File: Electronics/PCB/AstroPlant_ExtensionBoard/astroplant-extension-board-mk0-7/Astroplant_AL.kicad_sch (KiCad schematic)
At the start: 25 parts, among them J1 JST_XH_Relays, J10 JST_XH_UART, J11 JST_HX_2, J2 2x40 2.5mm Header, J3 JST-XH_3, J4 JST-XH_3, J5 JST_HX_2, J7 JST-XH_3, J8 JST_HX_2, J9 JST-XH_3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

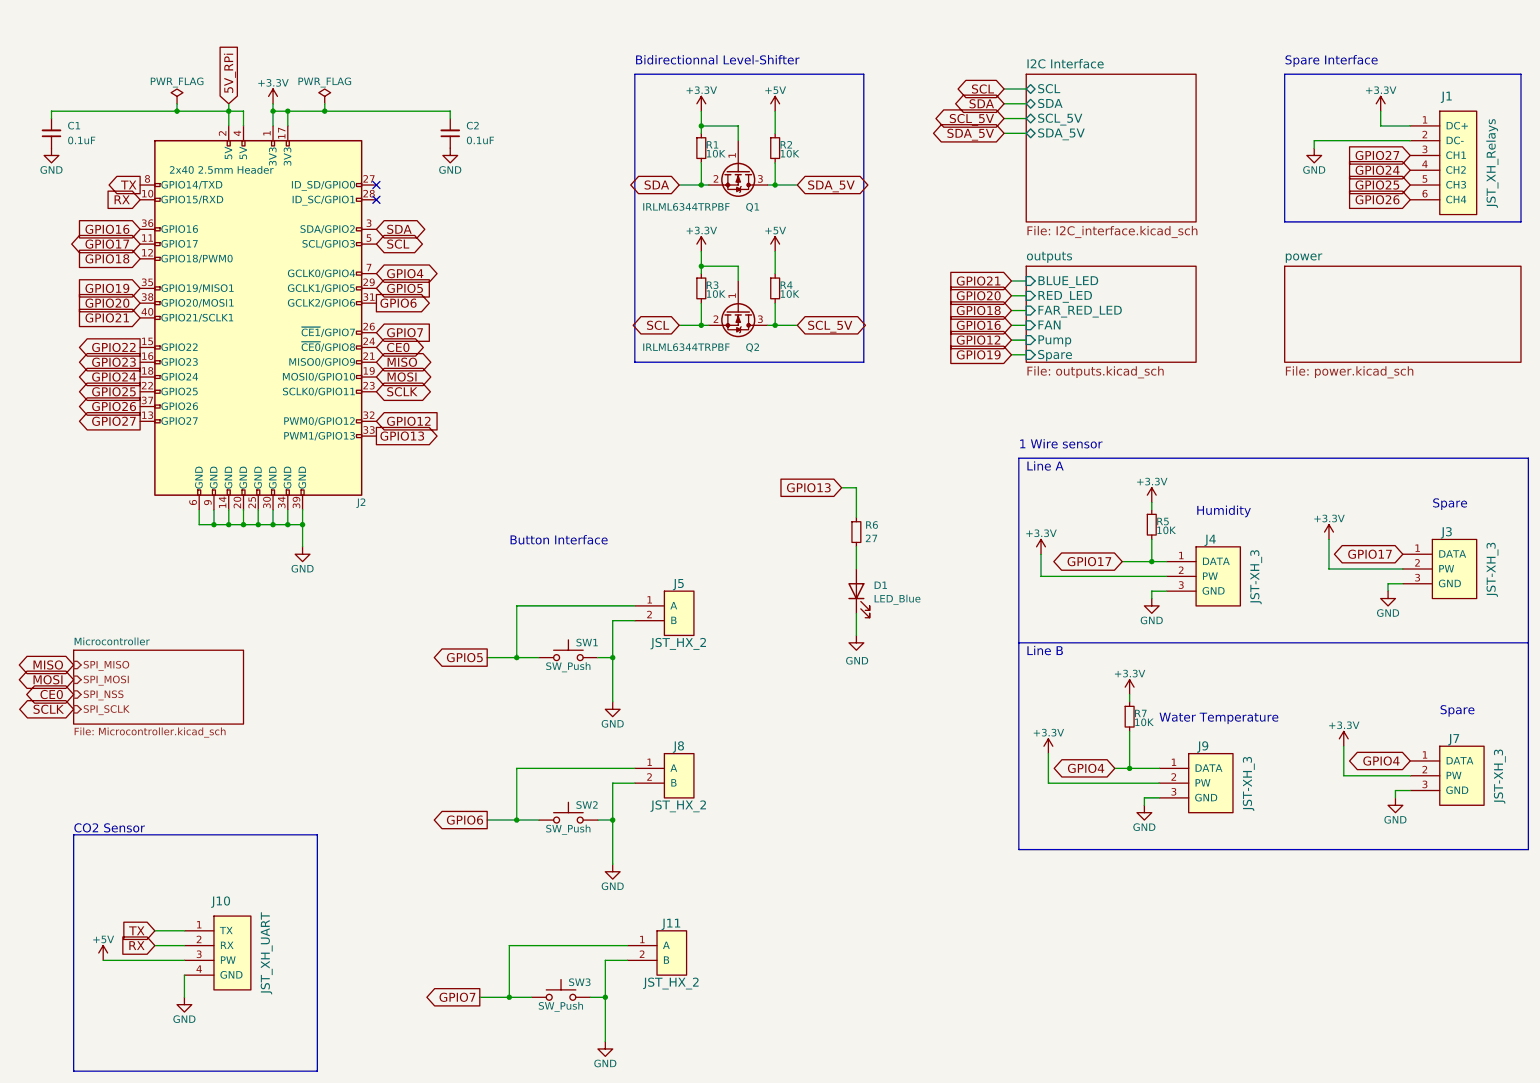
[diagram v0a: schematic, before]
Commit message: Update schematic and change library path
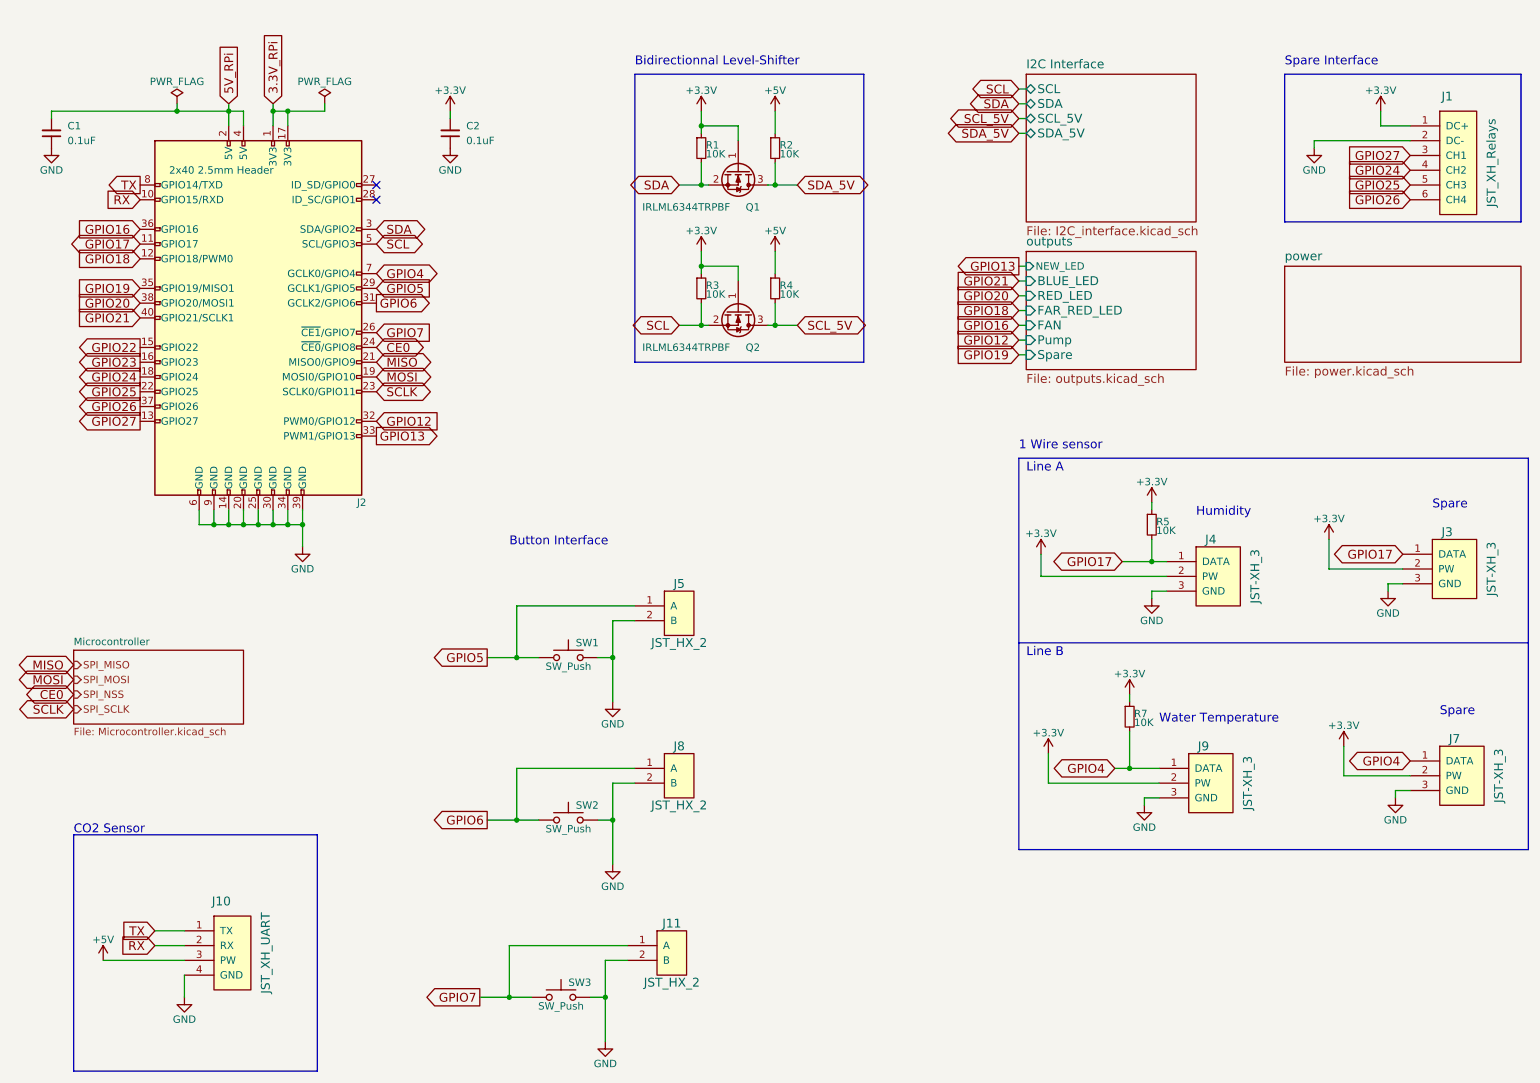
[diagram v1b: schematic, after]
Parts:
- removed D1: LED_Blue, LED_SMD:LED_0603_1608Metric, symbol Device:LED
- removed R6: 27, Resistor_SMD:R_0603_1608Metric, symbol Device:R_Small
- J1: footprint Connector_JST:JST_XH_B06B-XH-A_1x06_P2.50mm_Vertical -> SamacSys_Parts:SHDR6W64P0X250_1X6_1740X575X700P
- J10: footprint Connector_JST:JST_XH_B04B-XH-A_1x04_P2.50mm_Vertical -> SamacSys_Parts:B4BXHALFSN
- J11, J5, J8: footprint Connector_JST:JST_XH_B02B-XH-A_1x02_P2.50mm_Vertical -> SamacSys_Parts:SHDR2W64P0X250_1X2_740X575X700P
- J2: footprint footprints:Pin_Header_Straight_2x20_Pitch2.54mm -> SamacSys_Parts:HDRV40W64P254X254_2X20_5080X508X869P
- J3, J4, J7, J9: footprint Connector_JST:JST_XH_B03B-XH-A_1x03_P2.50mm_Vertical -> SamacSys_Parts:B3BXHALFSN
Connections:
- net +3V3: no longer J2.1 (3V3), J2.17 (3V3)
- new net 3.3V_RPi: J2.1 (3V3), J2.17 (3V3)
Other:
- sheet outputs ports: added NEW_LED; removed none

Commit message: Place components on PCB
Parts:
- removed C1, C2: 0.1uF, Capacitor_SMD:C_0805_2012Metric, symbol Device:C_Small
- removed R1, R2, R3, R4, R5, R7: 10K, Resistor_SMD:R_0805_2012Metric, symbol Device:R_Small
- added C9 (x2): 100nF, Capacitor_SMD:C_0603_1608Metric, symbol Device:C_Small
- added R24 (x6): 10k, Resistor_SMD:R_0603_1608Metric, symbol Device:R_Small
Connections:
- net +3V3: now also C9.1, R24.2, R24.2, R24.2, R24.2
- net +5V: now also R24.2, R24.2
- net 5V_RPi: now also C9.1
- net GND: now also C9.2, C9.2
- net GPIO17: now also R24.1
- net GPIO4: now also R24.1
- net SCL: now also R24.1
- net SCL_5V: now also R24.1
- net SDA: now also R24.1
- net SDA_5V: now also R24.1

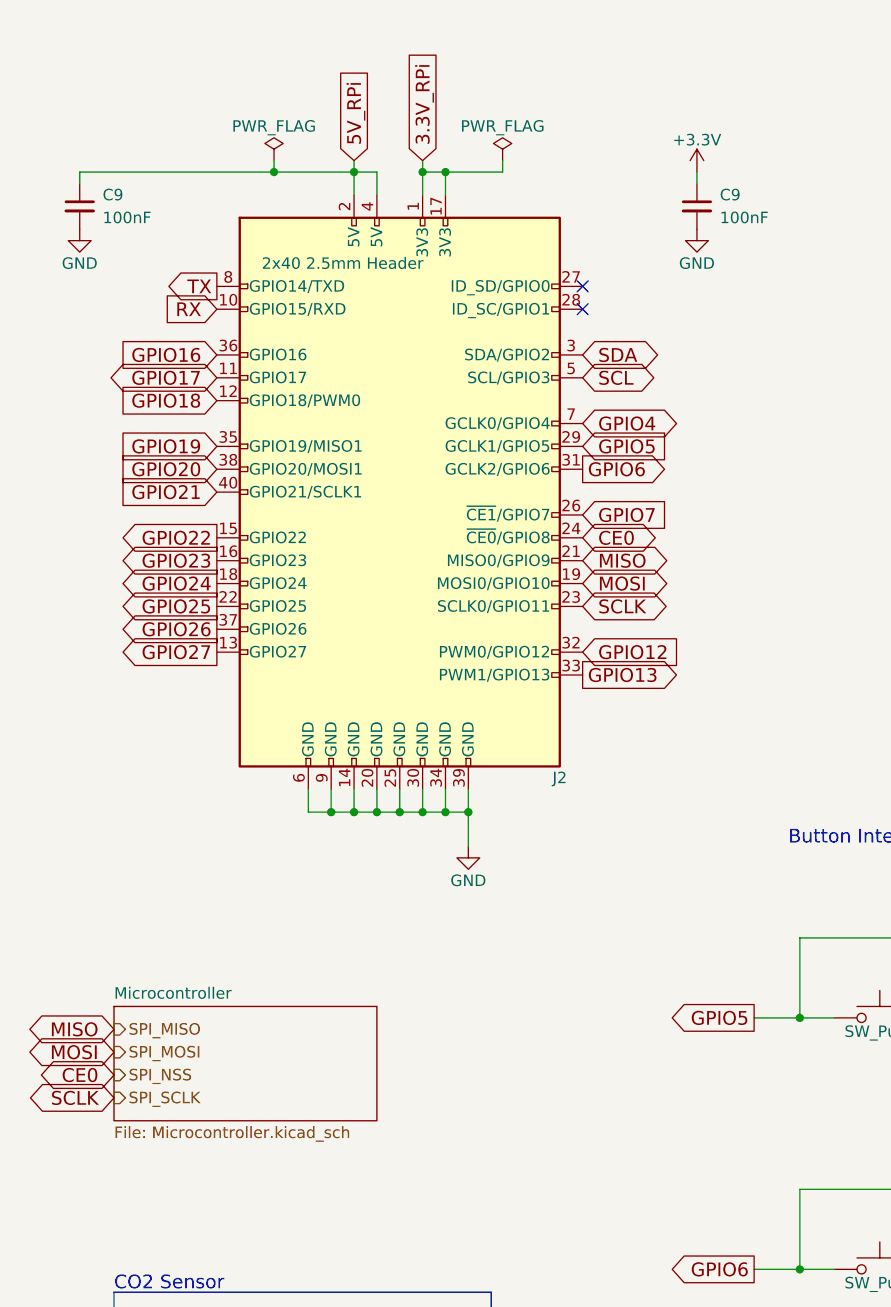
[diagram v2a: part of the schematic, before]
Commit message: Add route to PCB
Not the final version of the PCB, missing components for the antenna and also non-component things like the astroplant logo, the version and placement of the component designators.
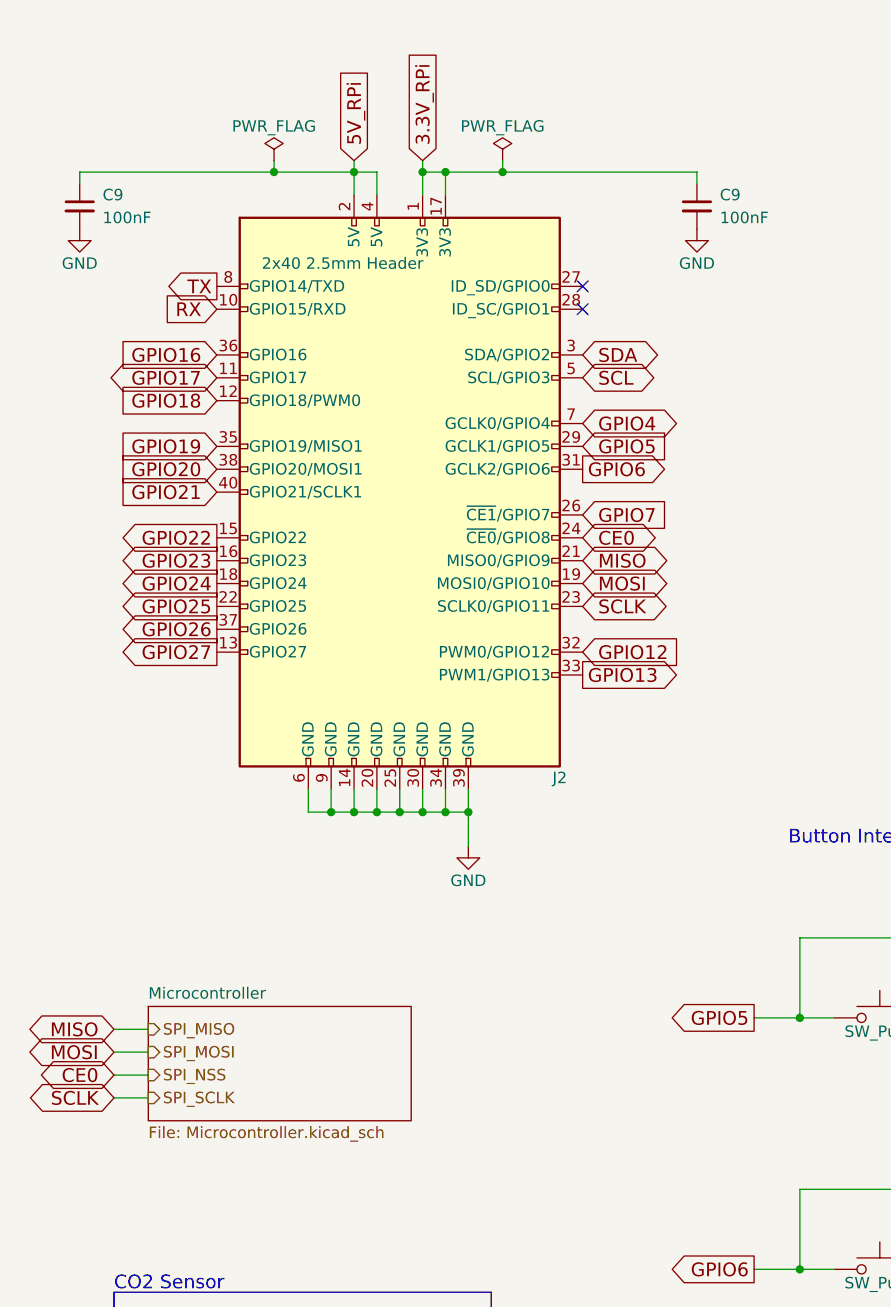
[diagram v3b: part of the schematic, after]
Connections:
- net +3V3: no longer C9.1
- net 3.3V_RPi: now also C9.1
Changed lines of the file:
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@@
   (junction (at 116.84 123.19) (diameter 0) (color 0 0 0 0)
+  )
+  (junction (at 67.31 29.21) (diameter 0) (color 0 0 0 0)
   )
   (junction (at 132.08 55.88) (diameter 0) (color 0 0 0 0)
@@
     (stroke (width 0) (type default))
   )
+  (wire (pts (xy 27.94 129.54) (xy 24.13 129.54))
+    (stroke (width 0) (type default))
+  )
   (wire (pts (xy 63.5 97.79) (xy 63.5 100.33))
     (stroke (width 0) (type default))
@@
     (stroke (width 0) (type default))
   )
+  (wire (pts (xy 27.94 124.46) (xy 24.13 124.46))
+    (stroke (width 0) (type default))
+  )
   (wire (pts (xy 132.08 62.23) (xy 132.08 66.04))
     (stroke (width 0) (type default))
   )
+  (wire (pts (xy 27.94 132.08) (xy 24.13 132.08))
+    (stroke (width 0) (type default))
+  )
   (wire (pts (xy 60.96 29.21) (xy 67.31 29.21))
     (stroke (width 0) (type default))
@@
     (stroke (width 0) (type default))
   )
+  (wire (pts (xy 27.94 127) (xy 24.13 127))
+    (stroke (width 0) (type default))
+  )
   (wire (pts (xy 50.8 100.33) (xy 50.8 97.79))
     (stroke (width 0) (type default))
@@
     (stroke (width 0) (type default))
   )
-  (wire (pts (xy 88.9 29.21) (xy 88.9 30.48))
-    (stroke (width 0) (type default))
-  )
   (wire (pts (xy 60.96 100.33) (xy 60.96 97.79))
     (stroke (width 0) (type default))
@@
     (stroke (width 0) (type default))
   )
+  (wire (pts (xy 88.9 30.48) (xy 88.9 29.21))
+    (stroke (width 0) (type default))
+  )
   (wire (pts (xy 114.3 151.13) (xy 116.84 151.13))
     (stroke (width 0) (type default))
@@
   )
   (polyline (pts (xy 186.69 88.9) (xy 186.69 156.21))
+    (stroke (width 0) (type default))
+  )
+  (wire (pts (xy 88.9 29.21) (xy 67.31 29.21))
     (stroke (width 0) (type default))
   )
@@
     )
   )
-  (hierarchical_label "SPI_MISO" (shape output) (at 24.13 124.46 0) (fields_autoplaced)
+  (hierarchical_label "SPI_MISO" (shape output) (at 27.94 124.46 0) (fields_autoplaced)
     (effects (font (size 1.27 1.27)) (justify left))
   )
-  (hierarchical_label "SPI_SCLK" (shape output) (at 24.13 132.08 0) (fields_autoplaced)
+  (hierarchical_label "SPI_SCLK" (shape output) (at 27.94 132.08 0) (fields_autoplaced)
     (effects (font (size 1.27 1.27)) (justify left))
   )
-  (hierarchical_label "SPI_NSS" (shape output) (at 24.13 129.54 0) (fields_autoplaced)
+  (hierarchical_label "SPI_NSS" (shape output) (at 27.94 129.54 0) (fields_autoplaced)
     (effects (font (size 1.27 1.27)) (justify left))
   )
-  (hierarchical_label "SPI_MOSI" (shape output) (at 24.13 127 0) (fields_autoplaced)
+  (hierarchical_label "SPI_MOSI" (shape output) (at 27.94 127 0) (fields_autoplaced)
     (effects (font (size 1.27 1.27)) (justify left))
   )
@@
     )
   )
-  (symbol (lib_id "Astroplant_VFR-rescue:+3.3V-power") (at 88.9 29.21 0) (unit 1)
-    (in_bom yes) (on_board yes) (dnp no)
-    (property "Reference" "#PWR0116" (at 88.9 33.02 0)
-      (effects (font (size 1.27 1.27)) hide)
-    )
-    (property "Value" "+3.3V" (at 88.9 25.654 0)
-      (effects (font (size 1.27 1.27)))
-    )
-    (property "Footprint" "" (at 88.9 29.21 0)
-      (effects (font (size 1.27 1.27)) hide)
-    )
-    (property "Datasheet" "" (at 88.9 29.21 0)
-      (effects (font (size 1.27 1.27)) hide)
-    )
-    (pin "1")
-    (instances
-      (project "Astroplant_VFR"
-        (path "/4e818498-015c-45b7-982b-80c19490efdc"
-          (reference "#PWR0116") (unit 1)
-        )
-      )
-      (project "Astroplant_AL"
-        (path "/51acab52-3cd6-4bba-9dee-c12efd332038"
-          (reference "#PWR014") (unit 1)
-        )
-        (path "/51acab52-3cd6-4bba-9dee-c12efd332038/5f0c961f-7fa6-4a15-8a74-755a432cc19e"
-          (reference "#PWR06") (unit 1)
-        )
-        (path "/51acab52-3cd6-4bba-9dee-c12efd332038/00000000-0000-0000-0000-00005a8053d4"
-          (reference "#PWR011") (unit 1)
-        )
-      )
-    )
-  )
   (symbol (lib_id "Device:R_Small") (at 144.78 35.56 180) (unit 1)
     (in_bom yes) (on_board yes) (dnp no) (fields_autoplaced)
@@
     )
   )
-  (sheet (at 24.13 121.92) (size 29.21 12.7) (fields_autoplaced)
+  (sheet (at 27.94 121.92) (size 29.21 12.7) (fields_autoplaced)
     (stroke (width 0.1524) (type solid))
     (fill (color 0 0 0 0.0000))
-    (property "Sheetname" "Microcontroller" (at 24.13 121.2084 0)
+    (property "Sheetname" "Microcontroller" (at 27.94 121.2084 0)
       (effects (font (size 1.27 1.27)) (justify left bottom))
     )
-    (property "Sheetfile" "Microcontroller.kicad_sch" (at 24.13 135.2046 0)
+    (property "Sheetfile" "Microcontroller.kicad_sch" (at 27.94 135.2046 0)
       (effects (font (size 1.27 1.27)) (justify left top))
     )

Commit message: Changed PCB, add a LED to simplify tests
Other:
- title: (none) -> Main sheet
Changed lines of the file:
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@@
 (kicad_sch (version 20230121) (generator eeschema)
   (paper "A4")
+  (title_block
+    (title "Main sheet")
+    (date "2023-10-13")
+    (rev "0.7")
+    (comment 1 "Aurélien Lesage")
+  )
   (junction (at 48.26 100.33) (diameter 0) (color 0 0 0 0)
   )
